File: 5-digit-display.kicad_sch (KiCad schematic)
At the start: 5 parts, among them U16 MAX7219, U17 5_digit_7_segment_display

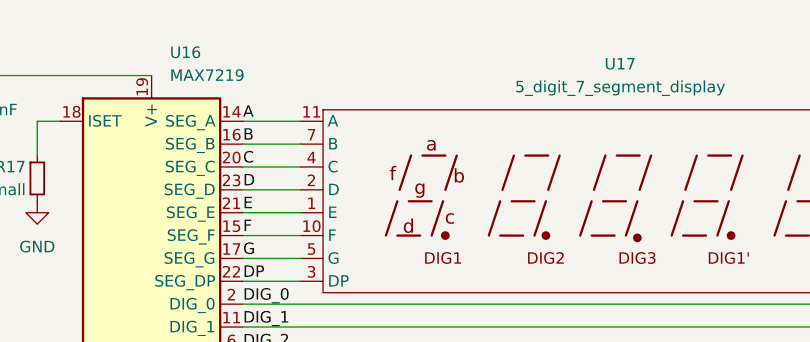
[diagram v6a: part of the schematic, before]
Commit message: Added dual encoder 3d model, fit everything on the board
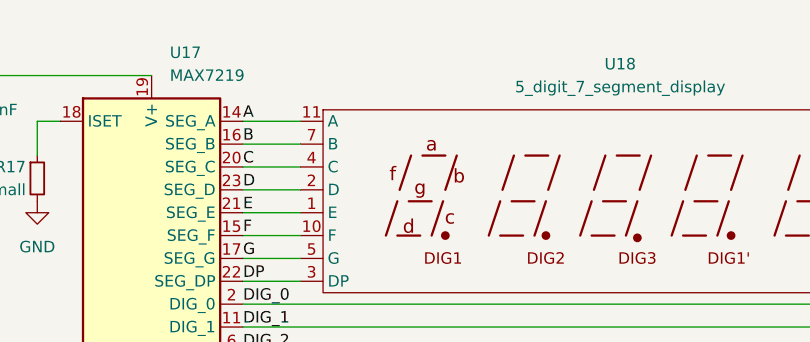
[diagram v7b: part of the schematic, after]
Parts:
- renumbered U16 to U17, U17 to U18
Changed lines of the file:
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@@
   (symbol (lib_id "power:GND") (at 64.77 92.71 0)
     (in_bom yes) (on_board yes) (fields_autoplaced)
-    (property "Reference" "#PWR042" (id 0) (at 64.77 99.06 0)
+    (property "Reference" "#PWR044" (id 0) (at 64.77 99.06 0)
       (effects (font (size 1.27 1.27)) hide)
     )
@@
   (symbol (lib_id "power:GND") (at 77.47 129.54 0)
     (in_bom yes) (on_board yes) (fields_autoplaced)
-    (property "Reference" "#PWR043" (id 0) (at 77.47 135.89 0)
+    (property "Reference" "#PWR045" (id 0) (at 77.47 135.89 0)
       (effects (font (size 1.27 1.27)) hide)
     )
@@
   (symbol (lib_id "Driver_LED:MAX7219") (at 77.47 104.14 0)
     (in_bom yes) (on_board yes) (fields_autoplaced)
-    (property "Reference" "U16" (id 0) (at 79.4894 76.2 0)
+    (property "Reference" "U17" (id 0) (at 79.4894 76.2 0)
       (effects (font (size 1.27 1.27)) (justify left))
     )
@@
   (symbol (lib_id "power:GND") (at 54.61 83.82 0)
     (in_bom yes) (on_board yes) (fields_autoplaced)
-    (property "Reference" "#PWR041" (id 0) (at 54.61 90.17 0)
+    (property "Reference" "#PWR043" (id 0) (at 54.61 90.17 0)
       (effects (font (size 1.27 1.27)) hide)
     )
@@
   (symbol (lib_id "power:+5V") (at 54.61 78.74 0)
     (in_bom yes) (on_board yes) (fields_autoplaced)
-    (property "Reference" "#PWR040" (id 0) (at 54.61 82.55 0)
+    (property "Reference" "#PWR042" (id 0) (at 54.61 82.55 0)
       (effects (font (size 1.27 1.27)) hide)
     )
@@
   (symbol (lib_id "Generic-radio-stack:5_digit_7_segment_display") (at 129.54 92.71 0)
     (in_bom yes) (on_board yes) (fields_autoplaced)
-    (property "Reference" "U17" (id 0) (at 129.54 77.47 0))
+    (property "Reference" "U18" (id 0) (at 129.54 77.47 0))
     (property "Value" "5_digit_7_segment_display" (id 1) (at 129.54 80.01 0))
     (property "Footprint" "Generic-radio-stack:5 digit (3+2) 7 segment LED display" (id 2) (at 129.54 106.68 0)

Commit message: Add mounting holes
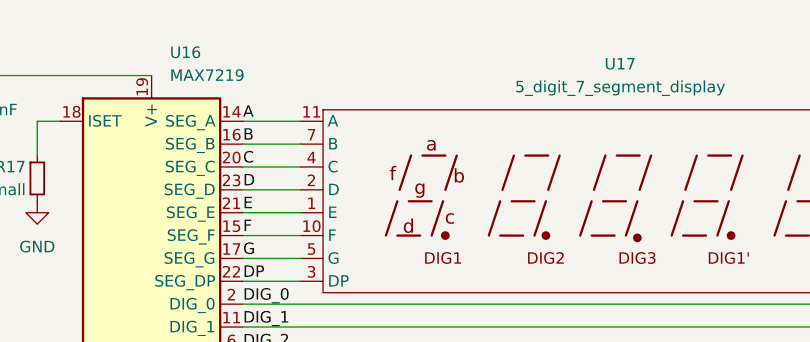
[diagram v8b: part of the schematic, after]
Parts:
- renumbered U17 to U16, U18 to U17
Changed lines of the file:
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@@
   (symbol (lib_id "power:GND") (at 64.77 92.71 0)
     (in_bom yes) (on_board yes) (fields_autoplaced)
-    (property "Reference" "#PWR044" (id 0) (at 64.77 99.06 0)
+    (property "Reference" "#PWR042" (id 0) (at 64.77 99.06 0)
       (effects (font (size 1.27 1.27)) hide)
     )
@@
   (symbol (lib_id "power:GND") (at 77.47 129.54 0)
     (in_bom yes) (on_board yes) (fields_autoplaced)
-    (property "Reference" "#PWR045" (id 0) (at 77.47 135.89 0)
+    (property "Reference" "#PWR043" (id 0) (at 77.47 135.89 0)
       (effects (font (size 1.27 1.27)) hide)
     )
@@
   (symbol (lib_id "Driver_LED:MAX7219") (at 77.47 104.14 0)
     (in_bom yes) (on_board yes) (fields_autoplaced)
-    (property "Reference" "U17" (id 0) (at 79.4894 76.2 0)
+    (property "Reference" "U16" (id 0) (at 79.4894 76.2 0)
       (effects (font (size 1.27 1.27)) (justify left))
     )
@@
   (symbol (lib_id "power:GND") (at 54.61 83.82 0)
     (in_bom yes) (on_board yes) (fields_autoplaced)
-    (property "Reference" "#PWR043" (id 0) (at 54.61 90.17 0)
+    (property "Reference" "#PWR041" (id 0) (at 54.61 90.17 0)
       (effects (font (size 1.27 1.27)) hide)
     )
@@
   (symbol (lib_id "power:+5V") (at 54.61 78.74 0)
     (in_bom yes) (on_board yes) (fields_autoplaced)
-    (property "Reference" "#PWR042" (id 0) (at 54.61 82.55 0)
+    (property "Reference" "#PWR040" (id 0) (at 54.61 82.55 0)
       (effects (font (size 1.27 1.27)) hide)
     )
@@
   (symbol (lib_id "Generic-radio-stack:5_digit_7_segment_display") (at 129.54 92.71 0)
     (in_bom yes) (on_board yes) (fields_autoplaced)
-    (property "Reference" "U18" (id 0) (at 129.54 77.47 0))
+    (property "Reference" "U17" (id 0) (at 129.54 77.47 0))
     (property "Value" "5_digit_7_segment_display" (id 1) (at 129.54 80.01 0))
     (property "Footprint" "Generic-radio-stack:5 digit (3+2) 7 segment LED display" (id 2) (at 129.54 106.68 0)
